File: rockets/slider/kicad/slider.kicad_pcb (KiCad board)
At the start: 2 copper layers, 54.6 x 91.4 mm, 43 parts, among them J1 I2C Breakout, J2 SPI Breakout, J3 SWD Breakout, J4 Pyro 1 Terminal, M1 Servo X, M2 Servo Y, Q1 IRF540N, Q2 IRF540N, Q3 IRF540N, SW1 SW_PWR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

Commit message: loads of pcb shiz
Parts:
- removed D2: LED (GRN), LED_THT:LED_D5.0mm
- removed D3, D4: LED (YLO), LED_THT:LED_D5.0mm
- removed J3: SWD Breakout, Connector_PinHeader_2.54mm:PinHeader_1x03_P2.54mm_Vertical
- removed NT2: Net-Tie_2, NetTie:NetTie-2_SMD_Pad0.5mm
- removed R4, R5, R6: 220, Resistor_THT:R_Axial_DIN0207_L6.3mm_D2.5mm_P7.62mm_Horizontal
- added H1: MountingHole, MountingHole:MountingHole_3mm, F.Cu at (204.8, 137.0)
- added H2: MountingHole, MountingHole:MountingHole_3mm, F.Cu at (204.8, 54.5)
- BT1: footprint TerminalBlock_4Ucon:TerminalBlock_4Ucon_1x02_P3.50mm_Horizontal -> TerminalBlock_Phoenix:TerminalBlock_Phoenix_PT-1,5-2-3.5-H_1x02_P3.50mm_Horizontal
- C2, C3: value 470uF -> 100uF; footprint Capacitor_THT:CP_Radial_D10.0mm_P2.50mm -> Capacitor_THT:CP_Radial_D6.3mm_P2.50mm
- D5: footprint Diode_THT:D_DO-35_SOD27_P10.16mm_Horizontal -> Diode_THT:D_DO-35_SOD27_P7.62mm_Horizontal
- SW1: value SW_PWR -> SW_SPDT; footprint Connector_PinHeader_2.54mm:PinHeader_1x03_P2.54mm_Vertical -> digikey-footprints:Toggle_Switch_100SP1T1B4M2QE
- SW2: value SW_ARM -> SW_SPDT; footprint Connector_PinHeader_2.54mm:PinHeader_1x03_P2.54mm_Vertical -> digikey-footprints:Toggle_Switch_100SP1T1B4M2QE
- U4: footprint RPi_Pico:RPi_Pico_SMD_TH -> RPi_Pico:RPi_Pico_TH_Perfboard
- moved NT1 191.6 mm to (224.3, 86.7)
- moved U4 186.2 mm to (205.2, 104.5), turned to 90 degrees
- moved C3 180.1 mm to (250.9, 114.7), turned to 90 degrees
- moved U3 179.2 mm to (243.3, 109.6), turned to 270 degrees
- moved S1 177.7 mm to (235.6, 77.1), turned to 270 degrees
- moved M1 175.9 mm to (233.1, 112.1)
- moved R8 174.9 mm to (220.4, 81.7), turned to 180 degrees
- moved M2 174.4 mm to (238.2, 112.1)
- moved U2 172.4 mm to (225.5, 109.6), turned to 270 degrees
- moved BT1 171.4 mm to (205.2, 124.8), turned to 315 degrees
- moved D5 170.1 mm to (207.7, 89.3)
- moved R7 167.2 mm to (212.8, 84.2), turned to 0 degrees
- moved Q1 166.5 mm to (235.7, 124.8)
- moved D1 166.2 mm to (215.4, 124.8)
- moved R2 164.6 mm to (243.3, 127.4)
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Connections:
- SW1 pad 1: Net-(SW1-Pad1) -> GND
- SW1 pad 2: +BATT -> ARM
- SW1 pad 3: Net-(BT1-Pad1) -> +3V3
- SW2 pad 1: GND -> +BATT
- SW2 pad 2: Net-(NT2-Pad1) -> Net-(BT1-Pad1)
- SW2 pad 3: +3V3 -> Net-(SW2-Pad3)
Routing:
- net GND: track 0.00 -> 0.78 mm
- net Net-(NT1-Pad2): track 0.00 -> 0.76 mm
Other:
- board size 54.6 x 91.4 mm -> 55 x 90.8 mm
- board text added: "X"
- board text added: "Z"
- board text removed: "Battery Input"
- board text removed: "Better Footprint?"
- board text removed: "Servo X Power"
- board text removed: "Servo Z Power"
- board text removed: "uC Power"

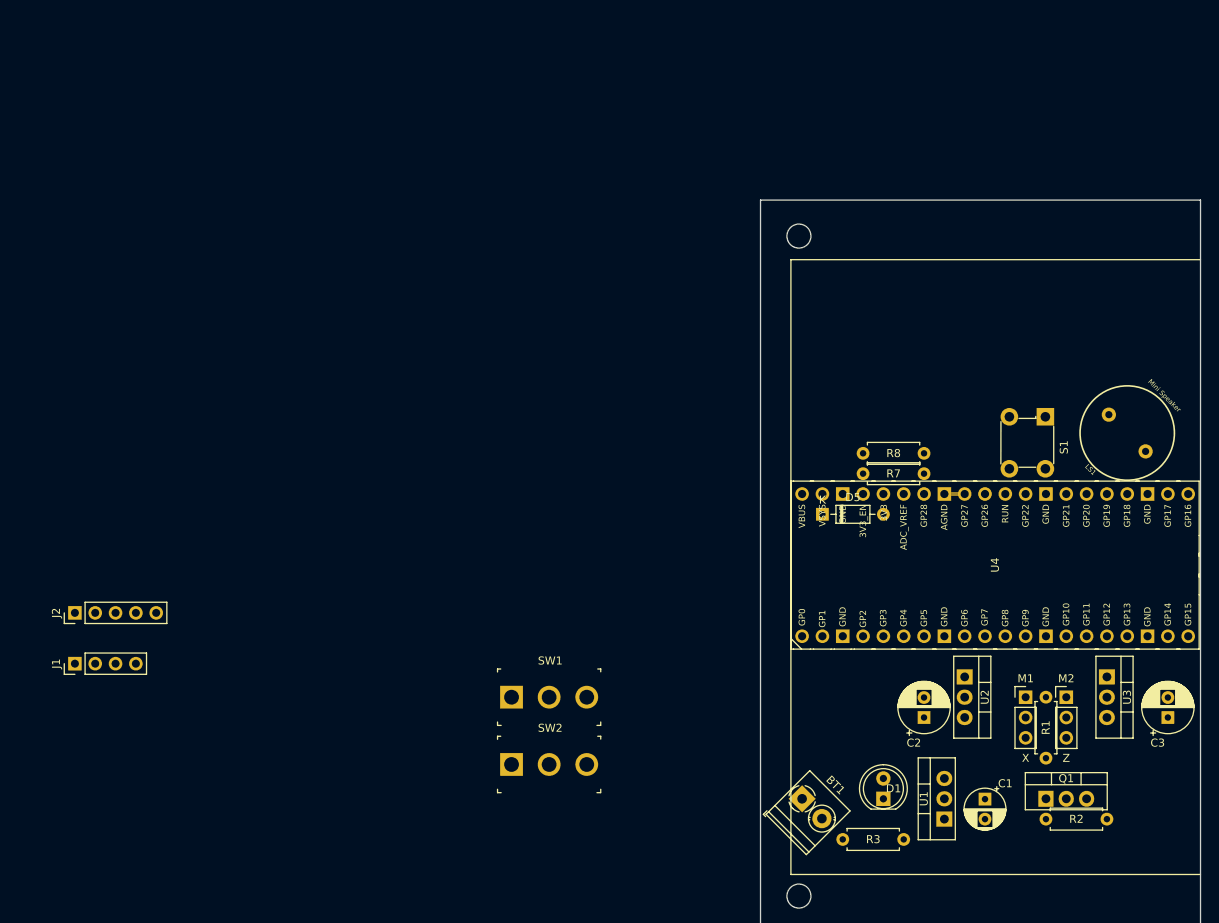
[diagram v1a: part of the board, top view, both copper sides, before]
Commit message: Lots of 3d models for kicad and rethinking the pcb design
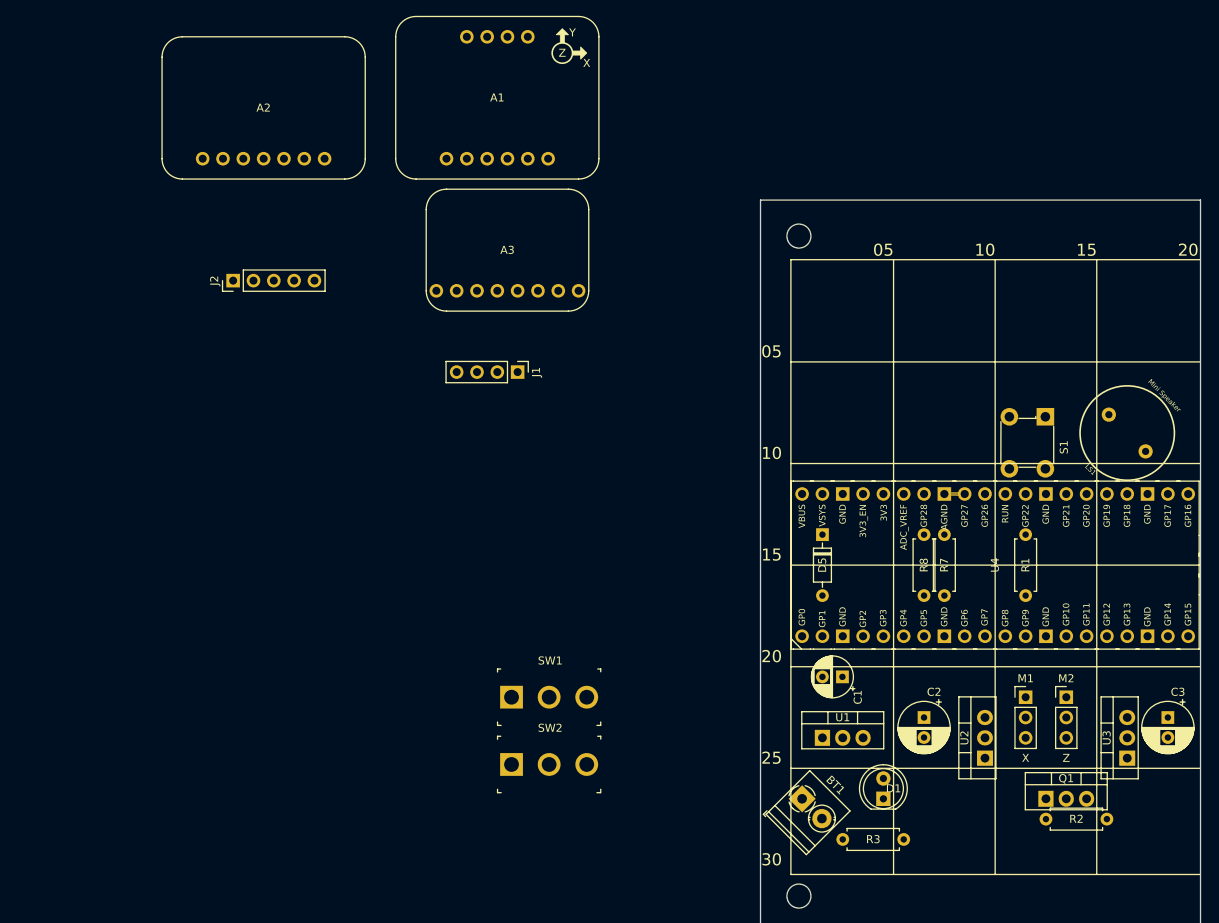
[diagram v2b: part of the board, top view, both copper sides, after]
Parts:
- added A1: Adafruit-BNO055, slider:Adafruit-BNO055, F.Cu at (167.1, 37.2)
- added A2: Adafruit-BMP280, slider:Adafruit-BMP280, F.Cu at (137.9, 38.5)
- added A3: MB85RC256V, slider:Adafruit-MB85RC256V, F.Cu at (168.4, 56.3)
- moved J1 66.3 mm to (169.6, 71.5), turned to 270 degrees
- moved J2 46.0 mm to (134.1, 60.1)
- moved C1 23.5 mm to (210.2, 109.6), turned to 180 degrees
- moved R1 20.5 mm to (233.1, 99.4)
- moved R7 18.3 mm to (223.0, 99.4), turned to 90 degrees
- moved U1 18.3 mm to (207.7, 117.2), turned to 0 degrees
- moved U2 10.5 mm to (228.1, 119.8), turned to 90 degrees
- moved U3 10.5 mm to (245.8, 119.8), turned to 90 degrees
- moved R8 10.2 mm to (220.4, 91.8), turned to 270 degrees
- moved D5 2.54 mm to (207.7, 91.8), turned to 270 degrees
- turned C2 to 270 degrees
- turned C3 to 270 degrees
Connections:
- J2 pad 2: SPI0_SCK -> SPI0_RX
- J2 pad 3: SPI0_TX -> SPI0_SCK
- J2 pad 4: SPI0_RX -> SPI0_TX
- U4 pad 22: Net-(U4-Pad22) -> BMP280_CS
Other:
- board text added: "05"
- board text added: "10"
- board text added: "15"
- board text added: "20"
- board text added: "25"
- board text added: "30"
- board text removed: "Servo Enable"

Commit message: Near v1 of board layout
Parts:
- removed A3: MB85RC256V, slider:Adafruit-MB85RC256V
- removed BZ1: Alarm Buzzer, slider:CE-C75-Piezo-Alarm
- removed J2: SPI Breakout, Connector_PinHeader_2.54mm:PinHeader_1x05_P2.54mm_Vertical
- removed J4: Pyro 1 Terminal, TerminalBlock_4Ucon:TerminalBlock_4Ucon_1x02_P3.50mm_Horizontal
- removed Q2, Q3: IRF540N, Package_TO_SOT_THT:TO-220-3_Vertical
- removed R10, R12: 2.2k, Resistor_THT:R_Axial_DIN0207_L6.3mm_D2.5mm_P7.62mm_Horizontal
- removed R11, R9: 220, Resistor_THT:R_Axial_DIN0207_L6.3mm_D2.5mm_P7.62mm_Horizontal
- removed R13: 220k, Resistor_THT:R_Axial_DIN0207_L6.3mm_D2.5mm_P7.62mm_Horizontal
- removed R14: 100k, Resistor_THT:R_Axial_DIN0207_L6.3mm_D2.5mm_P7.62mm_Horizontal
- removed SW2: SW_SPDT, digikey-footprints:Toggle_Switch_100SP1T1B4M2QE
- added D2: LED (RED), LED_THT:LED_D5.0mm, F.Cu at (235.7, 129.9)
- added D3: D_Schottky, Diode_THT:D_DO-35_SOD27_P7.62mm_Horizontal, F.Cu at (212.8, 119.8)
- added R4: 220, Resistor_THT:R_Axial_DIN0207_L6.3mm_D2.5mm_P7.62mm_Horizontal, F.Cu at (243.3, 124.8)
- added U5: FM25V20A-PG, cypress:FM25V20A, F.Cu at (250.9, 74.1)
- A1: value Adafruit-BNO055 -> BNO055; footprint slider:Adafruit-BNO055 -> adafruit:Adafruit_BNO055
- A2: value Adafruit-BMP280 -> BMP280; footprint slider:Adafruit-BMP280 -> adafruit:Adafruit_BMP280
- D1: value LED (RED) -> LED (YLO)
- J1: value I2C Breakout -> Parachute; footprint Connector_PinHeader_2.54mm:PinHeader_1x04_P2.54mm_Vertical -> Connector_PinHeader_2.54mm:PinHeader_1x03_P2.54mm_Vertical
- LS1: footprint Sparkfun Electromechanical:BUZZER-12MM -> SparkFun-Electromechanical:BUZZER-12MM
- SW1: footprint digikey-footprints:Toggle_Switch_100SP1T1B4M2QE -> digikey-footprints:Switch_Toggle_ATE1D-2M3-10-Z
- U4: footprint RPi_Pico:RPi_Pico_TH_Perfboard -> MCU_RaspberryPi_and_Boards:RPi_Pico_TH_Perfboard
- moved A2 102.4 mm to (235.7, 69.0)
- moved A1 62.0 mm to (210.3, 81.7)
- moved SW1 59.4 mm to (225.5, 129.9), turned to 180 degrees
- moved LS1 48.3 mm to (251.2, 127.1), turned to 45 degrees
- moved J1 40.2 mm to (207.7, 58.8), turned to 90 degrees
- moved R2 23.4 mm to (220.4, 122.3), turned to 0 degrees
- moved R1 18.0 mm to (235.7, 117.2)
- moved R7 7.62 mm to (215.4, 99.4)
- moved Q1 2.54 mm to (233.1, 124.8)
- moved C2 2.54 mm to (220.4, 112.1)
- moved C3 2.54 mm to (250.9, 112.1)
- moved M1 2.54 mm to (233.1, 109.6)
- moved M2 2.54 mm to (238.2, 109.6)
- moved U2 2.54 mm to (228.1, 117.2)
- moved U3 2.54 mm to (245.8, 117.2)
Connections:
- J1 pad 1: GND -> +BATT
- J1 pad 2: I2C0_SCL -> Parachute_Deploy
- J1 pad 3: I2C0_SDA -> GND
- U4 pad 10: Net-(U4-Pad10) -> ARM
- U4 pad 12: Net-(U4-Pad12) -> Servo_EN
- U4 pad 14: Pyro_1 -> PWM_Servo_X
- U4 pad 15: Pyro_1_Cont -> PWM_Servo_Z
- U4 pad 17: PWM_Buzzer -> Net-(U4-Pad17)
- U4 pad 19: Alarm_EN -> Net-(U4-Pad19)
- U4 pad 20: ARM -> PWM_Buzzer
- U4 pad 22: BMP280_CS -> Net-(U4-Pad22)
- U4 pad 26: PWM_Servo_Z -> FRAM_CS
- U4 pad 27: PWM_Servo_X -> BMP280_CS
- U4 pad 29: Servo_EN -> Parachute_Deploy
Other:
- board text removed: "NOT FINISHED"
- board text removed: "Pyro 1"

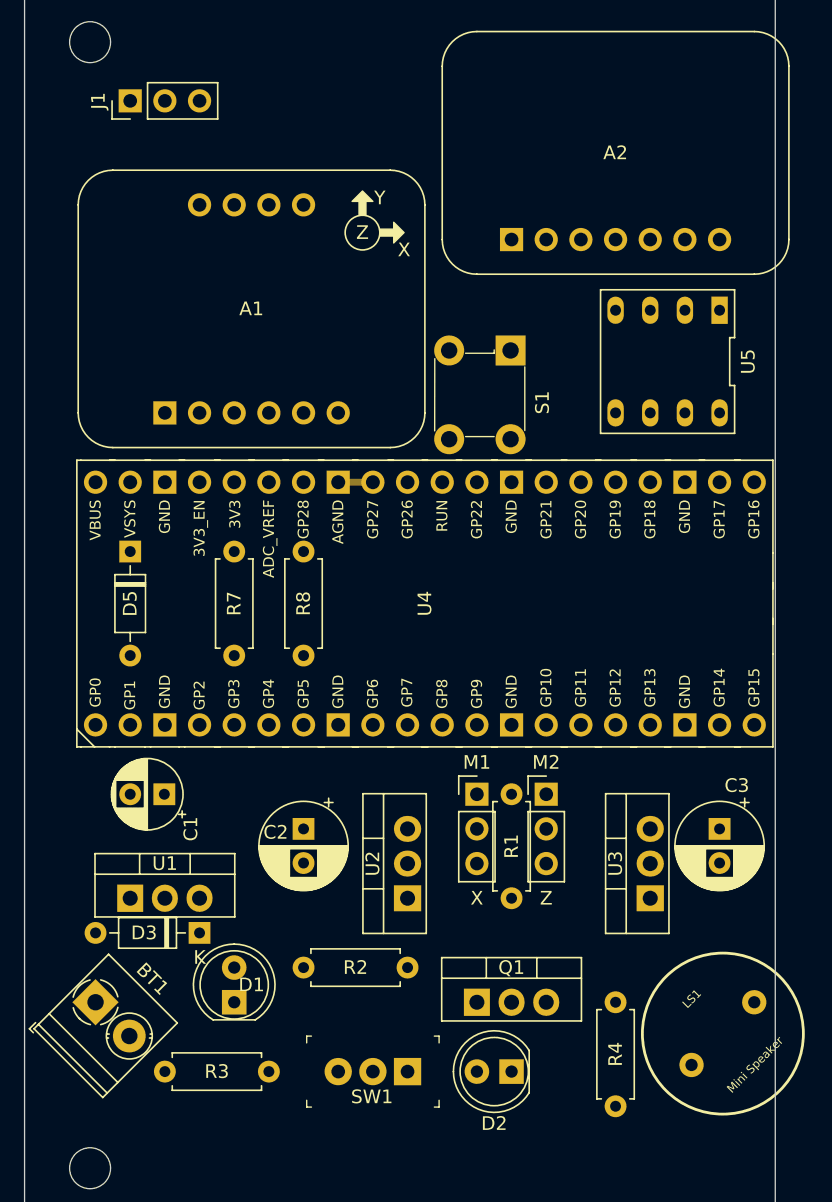
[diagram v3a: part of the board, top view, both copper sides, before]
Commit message: Routing and an additional pin header
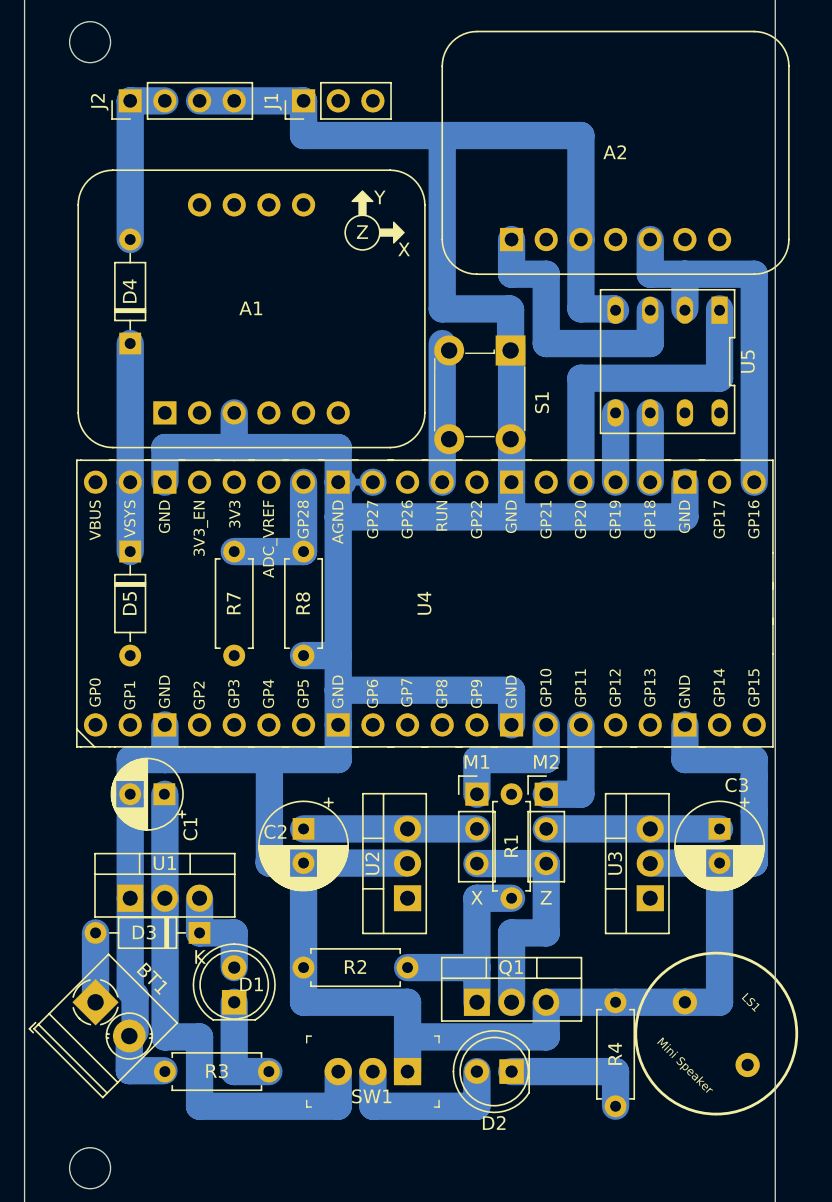
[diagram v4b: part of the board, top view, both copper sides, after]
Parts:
- added D4: D_Schottky, Diode_THT:D_DO-35_SOD27_P7.62mm_Horizontal, F.Cu at (207.7, 76.6)
- added J2: UC Debug PWR, Connector_PinHeader_2.54mm:PinHeader_1x04_P2.54mm_Vertical, F.Cu at (207.7, 58.8)
- NT1: moved to B.Cu
- moved J1 12.7 mm to (220.4, 58.8)
- moved LS1 0.49 mm to (250.7, 127.1), turned to 315 degrees
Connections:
- J1 pad 1: +BATT -> GND
- J1 pad 3: GND -> +BATT
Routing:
- net GND: track 0.78 -> 308.6 mm
- net +3V3: track 0.00 -> 58.3 mm
- net SPI0_RX: track 0.00 -> 27.9 mm
- net FRAM_CS: track 0.00 -> 22.9 mm
- net Servo_GND: track 0.00 -> 17.8 mm
- net Net-(Q1-Pad1): track 0.00 -> 15.2 mm
- net Net-(D4-Pad1): track 0.00 -> 15.2 mm
- net ARM: track 0.00 -> 12.7 mm
- net Servo_Z_VCC: track 0.00 -> 12.7 mm
- net Servo_X_VCC: track 0.00 -> 12.7 mm
- net Net-(D4-Pad2): track 0.00 -> 12.7 mm
- net Net-(D2-Pad1): track 0.00 -> 10.2 mm
- net PWM_Servo_X: track 0.00 -> 10.2 mm
- net RUN: track 0.00 -> 10.2 mm
- net V_BAT_Sense: track 0.00 -> 10.2 mm
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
